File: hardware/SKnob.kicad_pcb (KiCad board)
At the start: 4 copper layers, 50 x 17 mm, 69 parts, among them J1 USB_B_Micro, J2 Conn_01x02, J3 Conn_01x02, SW1 SW_Push, T1 LA_LOGO, T2 LA_LOGO, U1 STM32WB55Cx, U2 LIS2DE12TR, U3 USBLC6-2P6, Y1 32MHz, Y2 32.768kHz

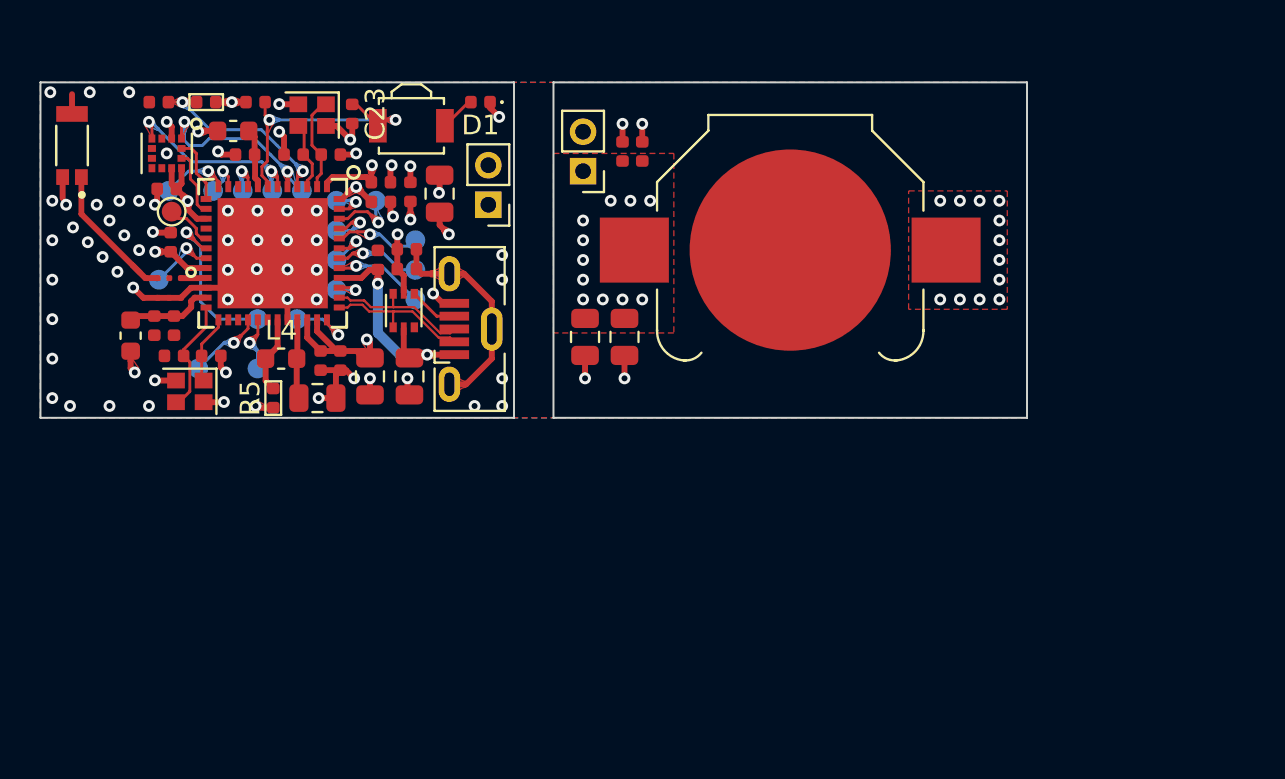
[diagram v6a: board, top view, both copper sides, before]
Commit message: added buzzer to PE4
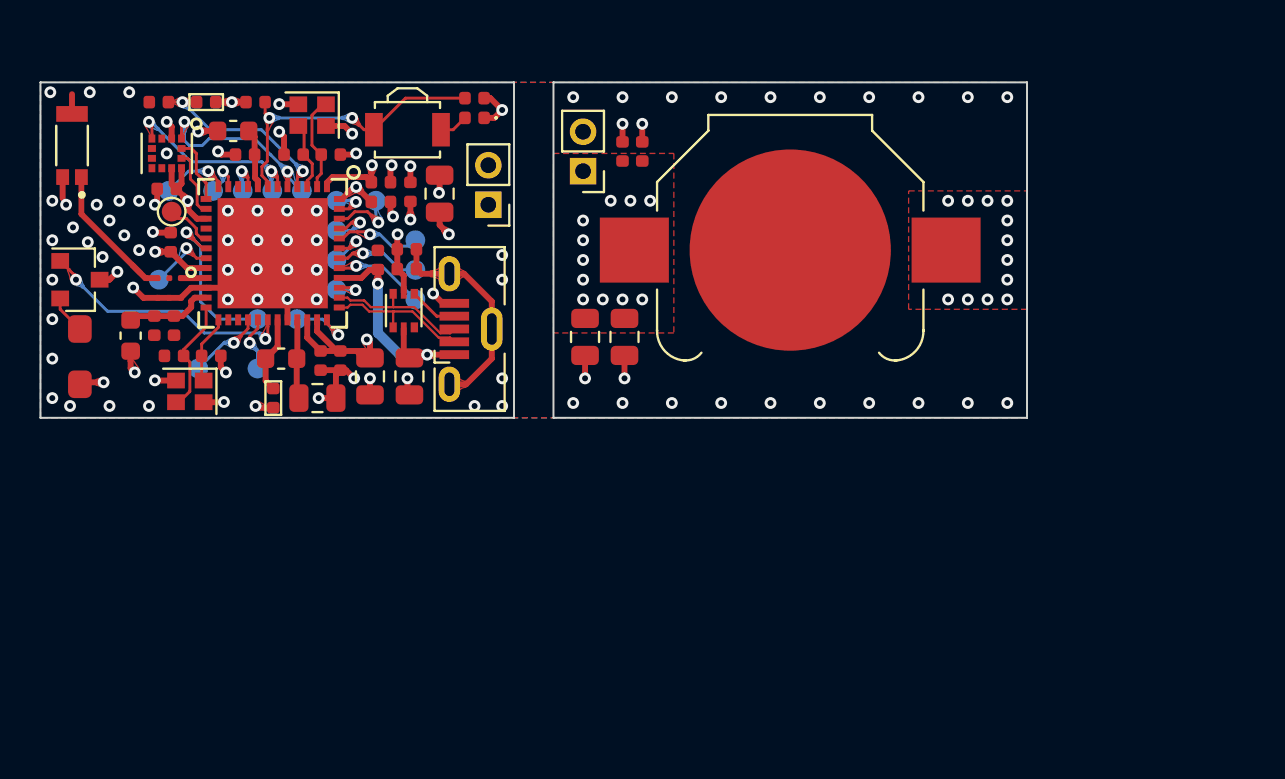
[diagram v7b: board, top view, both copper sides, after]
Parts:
- added BZ1: TE034003-1, SKnob:TE034003-1, F.Cu at (105.0, 85.9)
- added Q1: FDV301N, Package_TO_SOT_SMD:SOT-23, F.Cu at (105.0, 82.0)
- C1: value C -> 100nF
- R1: value R -> 10M
- T1: moved to B.Cu
- moved T1 20.2 mm to (121.0, 74.2), turned to 180 degrees
- moved C23 6.25 mm to (125.0, 72.8), turned to 0 degrees
- moved D1 0.85 mm to (125.0, 73.8)
- moved T2 0.30 mm to (150.3, 76.7)
- moved SW1 0.28 mm to (121.6, 74.4)
- moved QR***** 0.10 mm to (141.4, 80.5)
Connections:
- U1 pad 10: Net-(U1-Pad10) -> (no net)
- U1 pad 16: Net-(U1-Pad16) -> (no net)
- U1 pad 26: Net-(U1-Pad26) -> (no net)
- U1 pad 27: Net-(U1-Pad27) -> (no net)
- U1 pad 30: Net-(U1-Pad30) -> /BUZZER
- U2 pad 3: Net-(U2-Pad3) -> (no net)
- U3 pad 6: Net-(U3-Pad6) -> (no net)
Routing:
- net /BUZZER: track 0.00 -> 13.1 mm, vias 0 -> 2
- net Net-(BZ1-Pad2): track 0.00 -> 1.92 mm
- net /RST_N: track 13.8 -> 15.5 mm
- net GND: track 47.3 -> 48.8 mm, vias 71 -> 91
- net +BATT: track 29.5 -> 30.7 mm, vias 35 -> 36
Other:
- board text added: "LPUART"

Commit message: hardware Rev 1.0
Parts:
- C17, C19: value 15pF -> 9pF
- L1, L2: value 600R @ 100MHz -> 220 @ 100MHz
- Y2: footprint Crystal:Crystal_SMD_2016-4Pin_2.0x1.6mm -> Crystal:Crystal_SMD_2012-2Pin_2.0x1.2mm
- moved C23 6.40 mm to (118.8, 74.2), turned to 270 degrees
- moved D1 0.75 mm to (125.1, 73.0)
- moved Y2 0.52 mm to (116.8, 74.2)
- moved J2 0.50 mm to (125.8, 77.7)
- moved SW1 0.17 mm to (121.7, 74.2)
- renumbered BATT?1 to BATT1
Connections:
- Y2 pad 2: GND -> /OSC32_OUT
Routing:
- net /RST_N: track 15.5 -> 10.7 mm, vias 2 -> 0
- net GND: track 48.8 -> 44.9 mm, vias 91 -> 89
- net /OSC32_IN: track 4.84 -> 3.30 mm
